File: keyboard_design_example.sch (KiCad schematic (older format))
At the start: 34 parts, among them SW1 SW_PUSH, U1 ATmega32U4-AU, Y1 16MHz

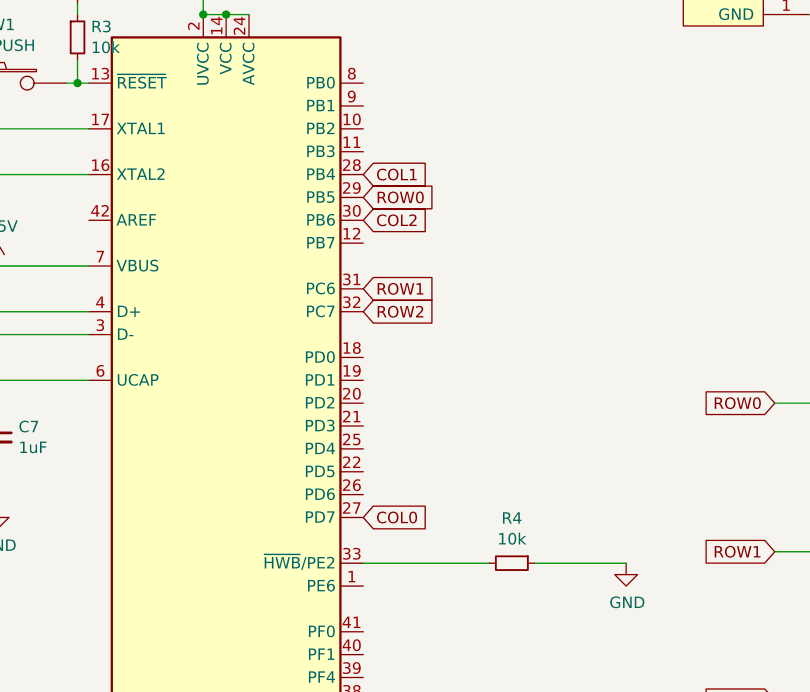
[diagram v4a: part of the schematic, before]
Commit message: Vertical MCU/usb
Made the usb and MCU face vertically and rewired the switch matrix to the mcu
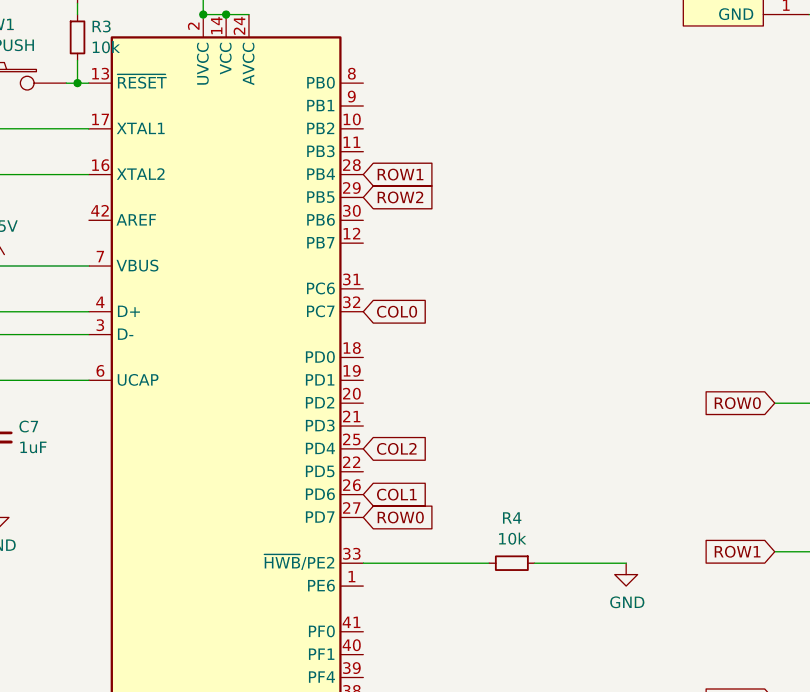
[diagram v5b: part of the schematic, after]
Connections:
- net COL0: now also U1.32 (PC7); no longer U1.27 (PD7)
- net COL1: now also U1.26 (PD6); no longer U1.28 (PB4)
- net COL2: now also U1.25 (PD4); no longer U1.30 (PB6)
- net ROW0: now also U1.27 (PD7); no longer U1.29 (PB5)
- net ROW1: now also U1.28 (PB4); no longer U1.31 (PC6)
- net ROW2: now also U1.29 (PB5); no longer U1.32 (PC7)
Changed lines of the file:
@@
 Text GLabel 9600 3100 1    50   Input ~ 0
 COL2
+Text GLabel 6350 2900 2    50   Input ~ 0
+ROW2
+Text GLabel 6350 2800 2    50   Input ~ 0
+ROW1
+Text GLabel 6350 4300 2    50   Input ~ 0
+ROW0
+Text GLabel 6350 4000 2    50   Input ~ 0
+COL2
+Text GLabel 6350 4200 2    50   Input ~ 0
+COL1
 Text GLabel 6350 3400 2    50   Input ~ 0
-ROW2
-Text GLabel 6350 3300 2    50   Input ~ 0
-ROW1
-Text GLabel 6350 2900 2    50   Input ~ 0
-ROW0
-Text GLabel 6350 3000 2    50   Input ~ 0
-COL2
-Text GLabel 6350 2800 2    50   Input ~ 0
-COL1
-Text GLabel 6350 4300 2    50   Input ~ 0
 COL0
 $EndSCHEMATC
